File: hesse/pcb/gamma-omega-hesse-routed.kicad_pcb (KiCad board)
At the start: 2 copper layers, 232.8 x 111.4 mm, 47 parts

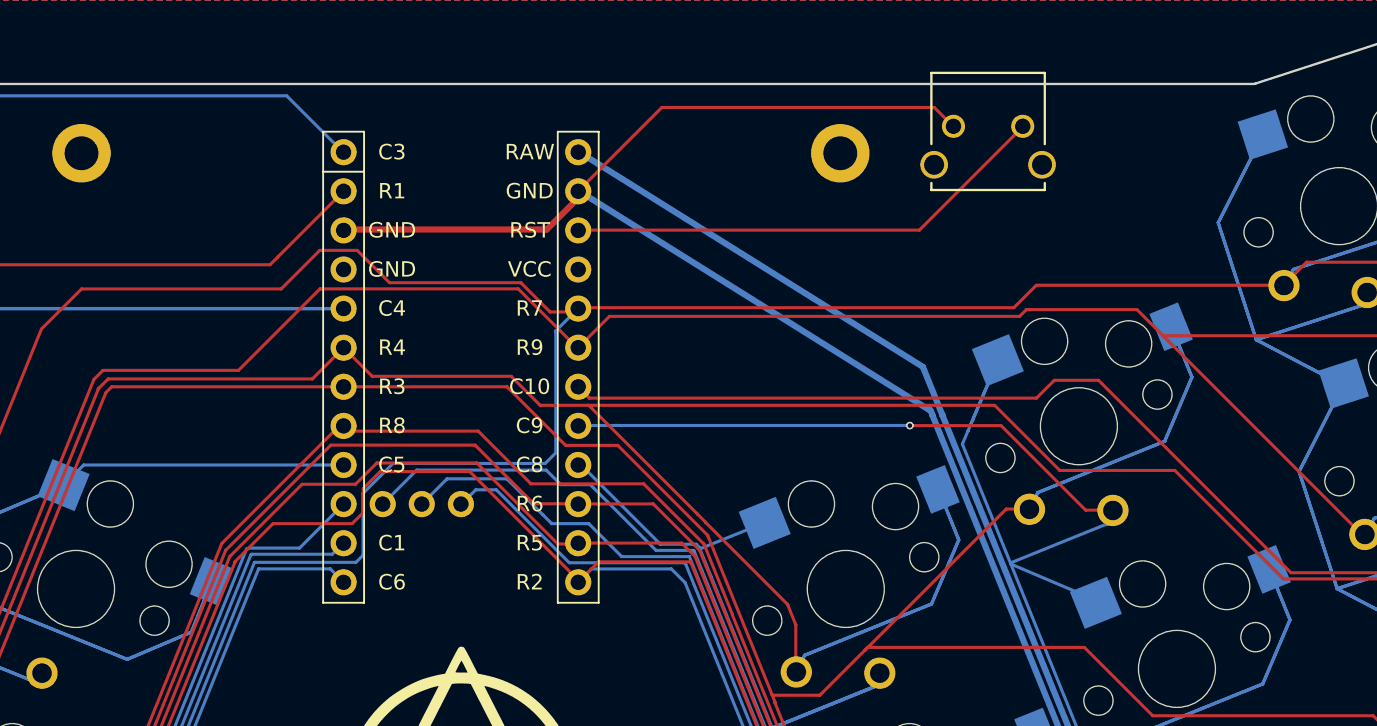
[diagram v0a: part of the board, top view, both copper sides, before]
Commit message: Use PCM_marbastlib-xp-promicroish:nice_nano_AH_USBup footprint
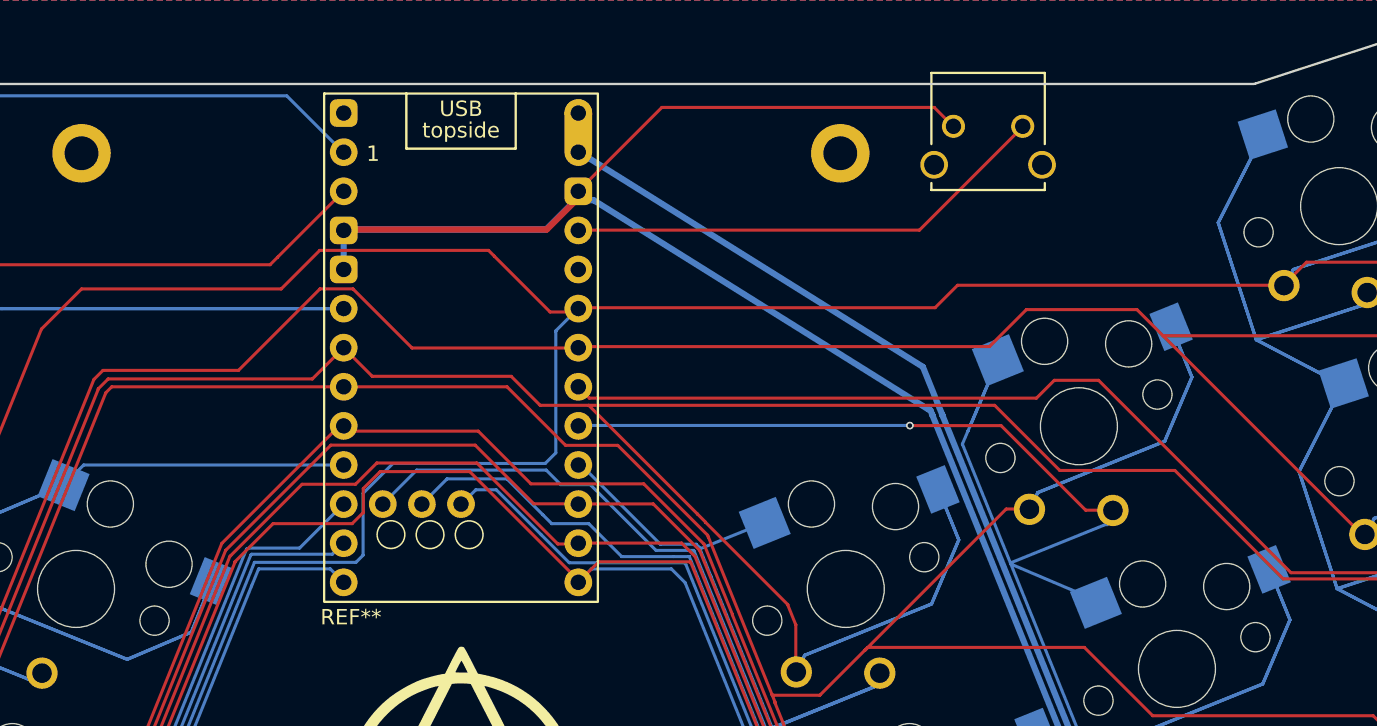
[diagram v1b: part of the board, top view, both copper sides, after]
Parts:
- removed MCU1: , ceoloide:mcu_nice_nano
- added REF**: nice_nano_AH_USBup, PCM_marbastlib-xp-promicroish:nice_nano_AH_USBup, F.Cu at (156.7, 68.2)
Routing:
- net GND: track 140.3 -> 159.6 mm
- net R9: track 339.2 -> 339.9 mm

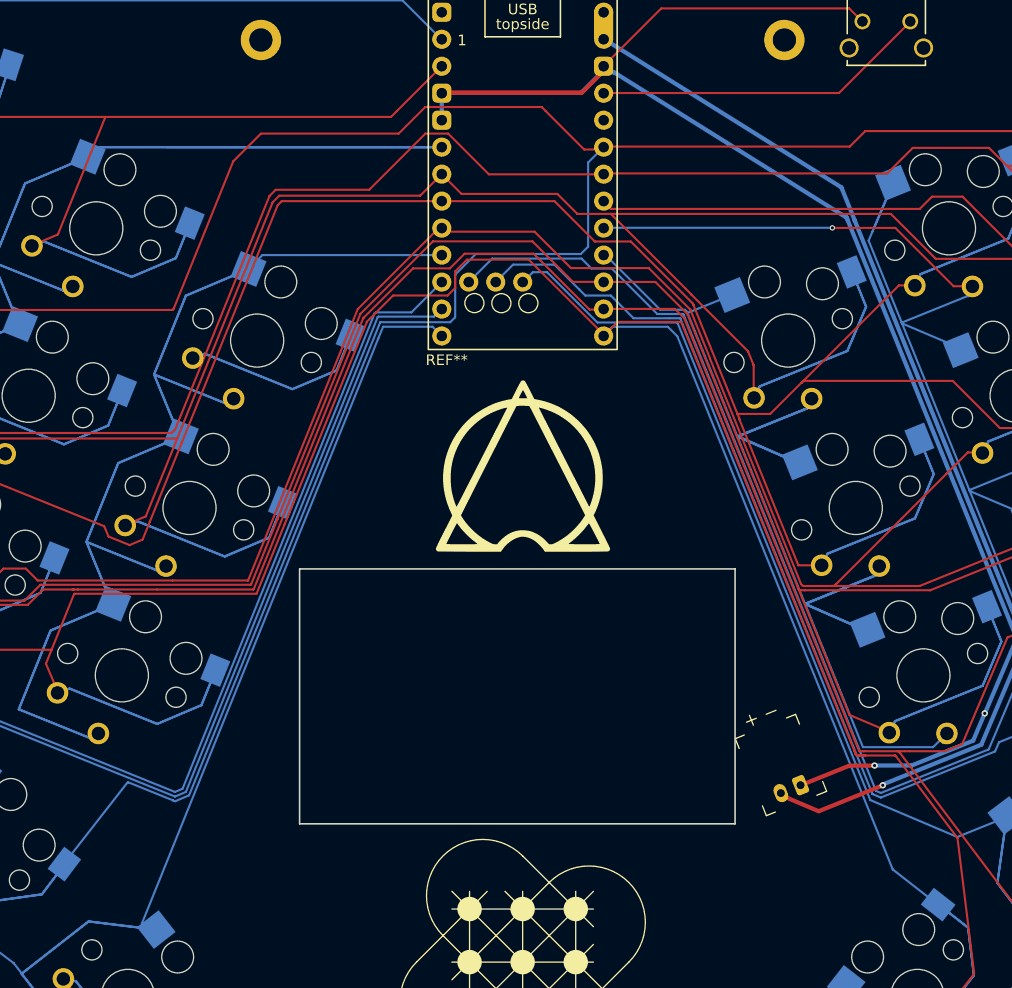
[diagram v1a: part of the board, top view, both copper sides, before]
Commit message: Polish routing at nice nano footprint; mark Supermini nRF52840 hole trio
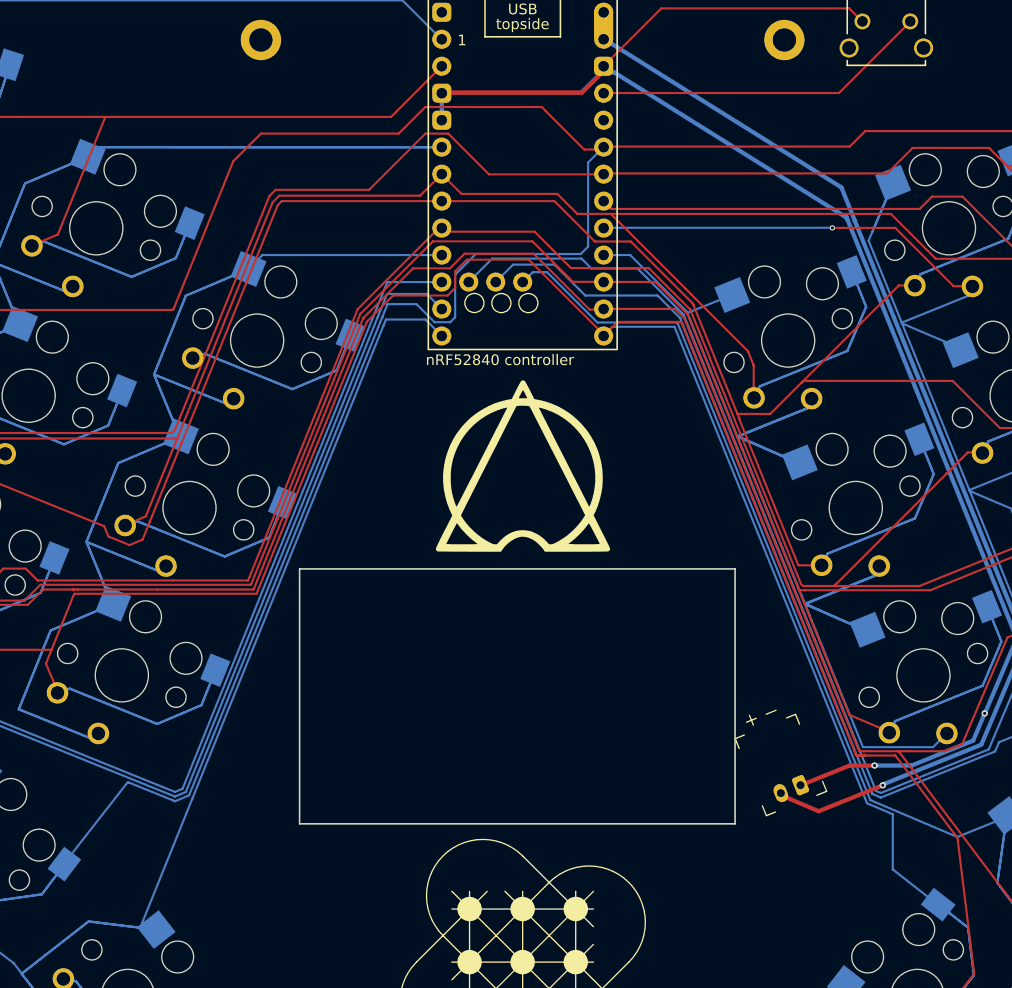
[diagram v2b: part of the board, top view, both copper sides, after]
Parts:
-  nRF52840 controller: renamed from REF**
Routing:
- net R7: track 405.8 -> 407.7 mm
- net C1: track 299.7 -> 301.4 mm
- net R2: track 467.1 -> 468.5 mm
- net GND: track 159.6 -> 158.7 mm
- net C8: track 156.7 -> 155.9 mm
- net C2: track 294.0 -> 294.8 mm
- net C6: track 231.8 -> 232.5 mm
- net R9: track 339.9 -> 339.4 mm

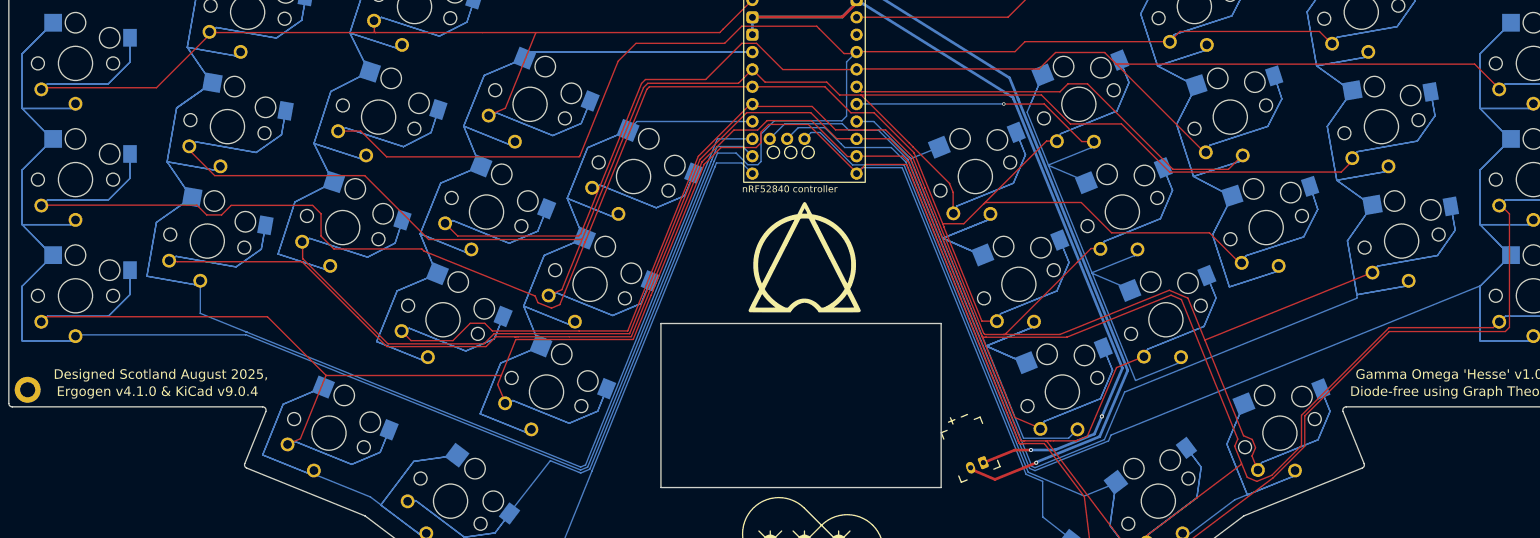
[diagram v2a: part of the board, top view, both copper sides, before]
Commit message: Add cutout to to reach Supermini nRF52840 hole trio (hackery)
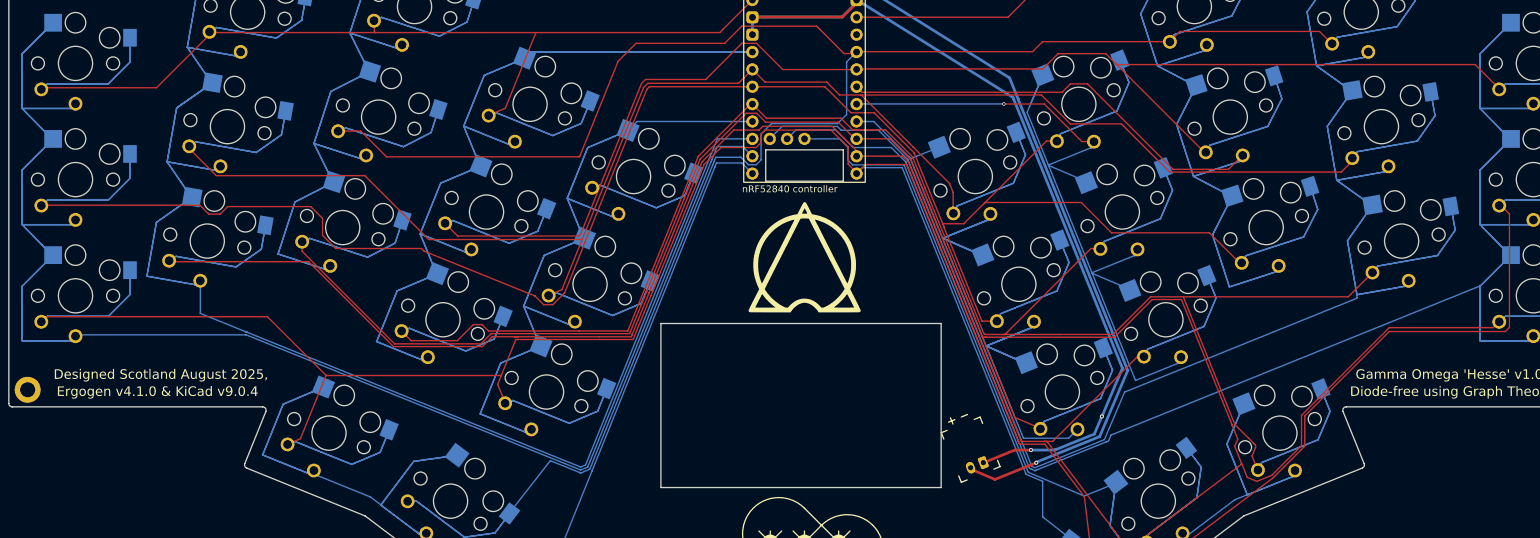
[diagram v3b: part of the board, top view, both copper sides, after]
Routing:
- net R8: track 377.6 -> 380.6 mm
- net R5: track 567.9 -> 566.2 mm
- net R3: track 397.6 -> 396.1 mm
- net R7: track 407.7 -> 406.8 mm
- net R6: track 435.7 -> 436.4 mm
- net R2: track 468.5 -> 469.0 mm
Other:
- outline, holes or cut-outs redrawn
